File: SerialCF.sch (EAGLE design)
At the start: 17 parts, among them IC1 XR-16C550P, IC2 74LS138N, T1 BC547, T2 BC547

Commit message: Update SerialCF
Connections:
- net A11: now also IC2A.G2A; no longer IC2A.G1
- net GND: now also IC2A.G1
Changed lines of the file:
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@@
 <instance part="P+11" gate="VCC" x="297.18" y="68.58"/>
 <instance part="GND9" gate="1" x="297.18" y="55.88"/>
-<instance part="GND13" gate="1" x="86.36" y="132.08"/>
+<instance part="GND13" gate="1" x="86.36" y="134.62"/>
 <instance part="T2" gate="G$1" x="111.76" y="-15.24"/>
 <instance part="R5" gate="G$1" x="101.6" y="-15.24"/>
@@
 </segment>
 <segment>
-<pinref part="GND13" gate="1" pin="GND"/>
-<wire x1="96.52" y1="134.62" x2="86.36" y2="134.62" width="0.1524" layer="91"/>
-</segment>
-<segment>
 <pinref part="GND3" gate="1" pin="GND"/>
 <pinref part="IC2" gate="P" pin="GND"/>
+</segment>
+<segment>
+<pinref part="IC2" gate="A" pin="G1"/>
+<pinref part="GND13" gate="1" pin="GND"/>
+<wire x1="96.52" y1="137.16" x2="86.36" y2="137.16" width="0.1524" layer="91"/>
 </segment>
 </net>
@@
 <pinref part="IC2" gate="A" pin="B"/>
 <wire x1="96.52" y1="147.32" x2="76.2" y2="147.32" width="0.1524" layer="91"/>
+<label x="88.9" y="147.32" size="1.778" layer="95"/>
 </segment>
 </net>
@@
 <pinref part="IC2" gate="A" pin="C"/>
 <wire x1="96.52" y1="144.78" x2="76.2" y2="144.78" width="0.1524" layer="91"/>
+<label x="88.9" y="144.78" size="1.778" layer="95"/>
 </segment>
 </net>
@@
 </segment>
 <segment>
-<pinref part="IC2" gate="A" pin="G1"/>
-<wire x1="96.52" y1="137.16" x2="76.2" y2="137.16" width="0.1524" layer="91"/>
-</segment>
-</net>
+<pinref part="IC2" gate="A" pin="G2A"/>
+<wire x1="96.52" y1="134.62" x2="91.44" y2="134.62" width="0.1524" layer="91"/>
+<wire x1="91.44" y1="134.62" x2="91.44" y2="129.54" width="0.1524" layer="91"/>
+<wire x1="91.44" y1="129.54" x2="76.2" y2="129.54" width="0.1524" layer="91"/>
+<label x="83.82" y="127" size="1.778" layer="95"/>
+</segment>
+</net>

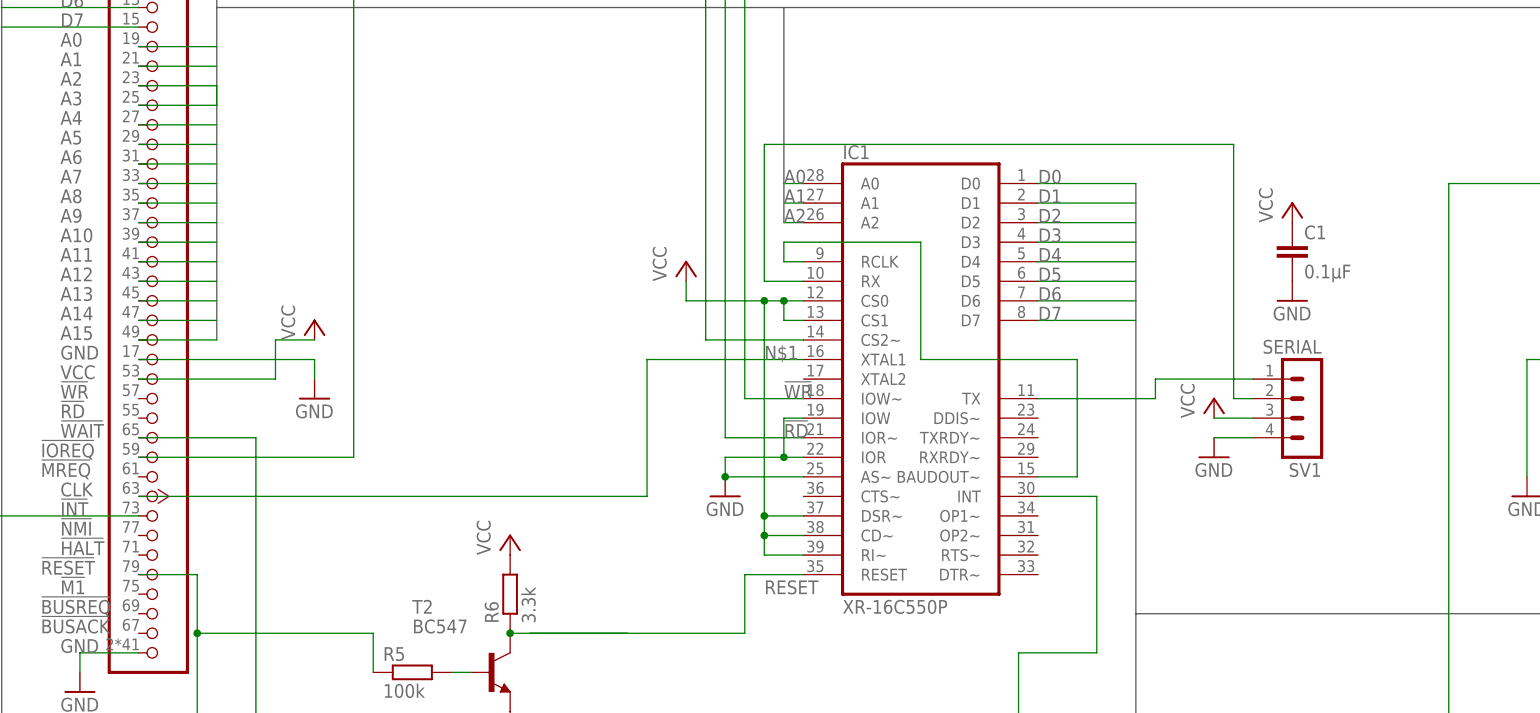
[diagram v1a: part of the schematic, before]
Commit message: Added Oscillator to SerialCF Board. And more Serial Pins
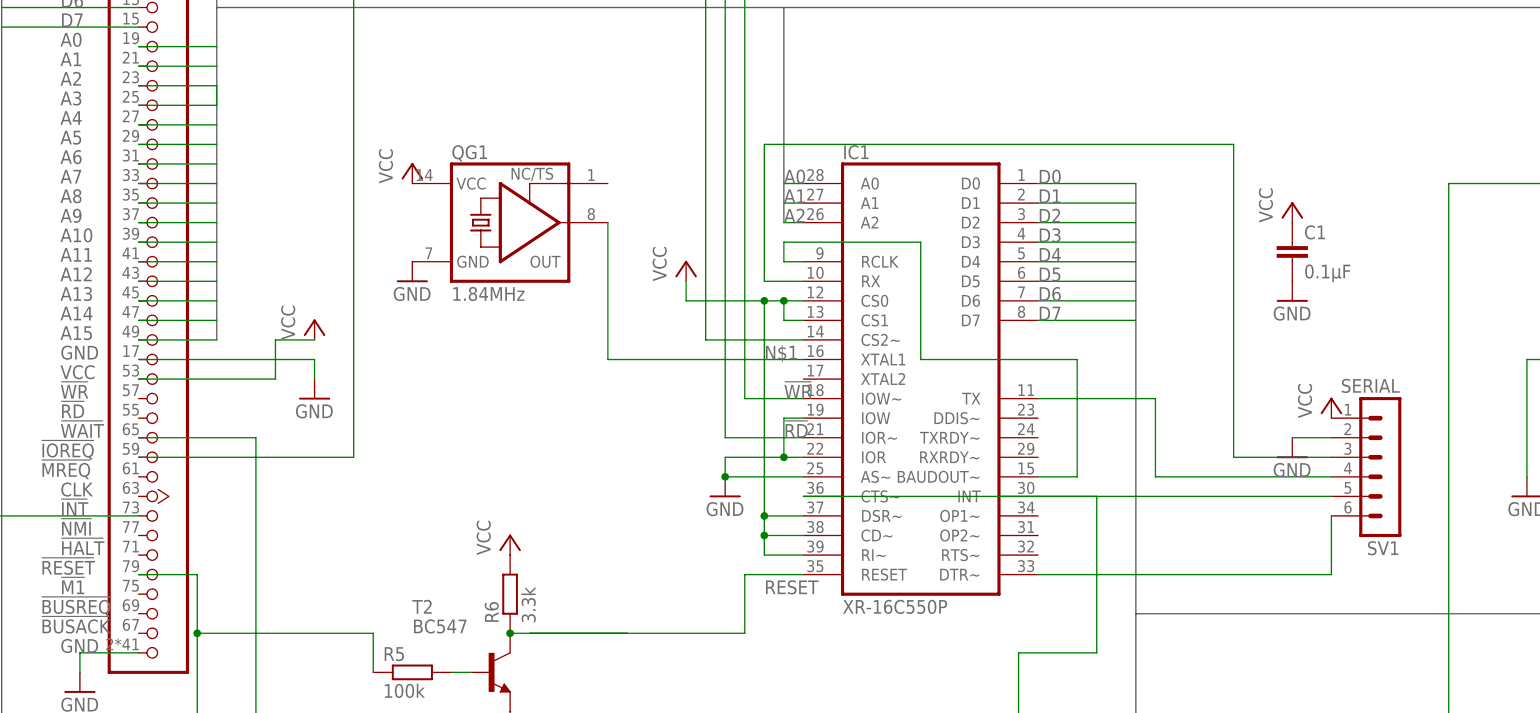
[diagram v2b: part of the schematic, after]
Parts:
- added QG1: 1.84MHz, crystal:XO-14
- SV1: device con-lstb:MA04-1 -> con-lstb:MA06-1
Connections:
- new net N$12: IC1G$1.CTS~, SV1.5
- new net N$14: IC1G$1.DTR~, SV1.6
- net GND: now also QG1.GND, SV1.2; no longer SV1.4
- net N$1: now also QG1.OUT; no longer JP1.CLK
- net N$11: now also SV1.4; no longer SV1.1
- net N$15: now also SV1.3; no longer SV1.2
- net VCC: now also QG1.VCC, SV1.1; no longer SV1.3
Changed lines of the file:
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@@
 <part name="GND7" library="supply1" deviceset="GND" device=""/>
 <part name="P+6" library="supply1" deviceset="VCC" device=""/>
-<part name="SV1" library="con-lstb" deviceset="MA04-1" device="" value="SERIAL"/>
+<part name="SV1" library="con-lstb" deviceset="MA06-1" device="" value="SERIAL"/>
 <part name="P+8" library="supply1" deviceset="VCC" device=""/>
 <part name="GND10" library="supply1" deviceset="GND" device=""/>
@@
 <part name="GND14" library="supply1" deviceset="GND" device=""/>
 <part name="IC2" library="74xx-eu" deviceset="74*138" device="N" technology="LS"/>
+<part name="QG1" library="crystal" deviceset="XO-" device="14" value="1.84MHz"/>
+<part name="P+10" library="supply1" deviceset="VCC" device=""/>
+<part name="GND8" library="supply1" deviceset="GND" device=""/>
 </parts>
 <sheets>
@@
 <instance part="GND7" gate="1" x="142.24" y="7.62"/>
 <instance part="P+6" gate="VCC" x="137.16" y="38.1"/>
-<instance part="SV1" gate="1" x="218.44" y="17.78" rot="R180"/>
-<instance part="P+8" gate="VCC" x="205.74" y="20.32"/>
-<instance part="GND10" gate="1" x="205.74" y="12.7"/>
+<instance part="SV1" gate="1" x="228.6" y="10.16" rot="R180"/>
+<instance part="P+8" gate="VCC" x="220.98" y="20.32"/>
+<instance part="GND10" gate="1" x="215.9" y="12.7"/>
 <instance part="SV2" gate="G$1" x="284.48" y="22.86" rot="R180"/>
 <instance part="R1" gate="G$1" x="299.72" y="2.54">
@@
 <instance part="IC2" gate="A" x="111.76" y="142.24"/>
 <instance part="IC2" gate="P" x="17.78" y="91.44"/>
+<instance part="QG1" gate="G$1" x="114.3" y="43.18"/>
+<instance part="P+10" gate="VCC" x="101.6" y="50.8"/>
+<instance part="GND8" gate="1" x="101.6" y="35.56"/>
 </instances>
 <busses>
@@
 </segment>
 <segment>
-<pinref part="SV1" gate="1" pin="3"/>
-<pinref part="P+8" gate="VCC" pin="VCC"/>
-<wire x1="210.82" y1="17.78" x2="205.74" y2="17.78" width="0.1524" layer="91"/>
-</segment>
-<segment>
 <pinref part="P+9" gate="VCC" pin="VCC"/>
 <wire x1="307.34" y1="33.02" x2="307.34" y2="25.4" width="0.1524" layer="91"/>
@@
 <pinref part="P+1" gate="VCC" pin="VCC"/>
 <pinref part="IC2" gate="P" pin="VCC"/>
+</segment>
+<segment>
+<pinref part="QG1" gate="G$1" pin="VCC"/>
+<pinref part="P+10" gate="VCC" pin="VCC"/>
+</segment>
+<segment>
+<pinref part="SV1" gate="1" pin="1"/>
+<pinref part="P+8" gate="VCC" pin="VCC"/>
 </segment>
 </net>
@@
 <wire x1="152.4" y1="10.16" x2="142.24" y2="10.16" width="0.1524" layer="91"/>
 <junction x="142.24" y="10.16"/>
-</segment>
-<segment>
-<pinref part="SV1" gate="1" pin="4"/>
-<pinref part="GND10" gate="1" pin="GND"/>
-<wire x1="210.82" y1="15.24" x2="205.74" y2="15.24" width="0.1524" layer="91"/>
 </segment>
 <segment>
@@
 <wire x1="96.52" y1="137.16" x2="86.36" y2="137.16" width="0.1524" layer="91"/>
 </segment>
+<segment>
+<pinref part="QG1" gate="G$1" pin="GND"/>
+<pinref part="GND8" gate="1" pin="GND"/>
+</segment>
+<segment>
+<pinref part="GND10" gate="1" pin="GND"/>
+<pinref part="SV1" gate="1" pin="2"/>
+<wire x1="215.9" y1="15.24" x2="220.98" y2="15.24" width="0.1524" layer="91"/>
+</segment>
 </net>
 <net name="!WR" class="0">
@@
 <net name="N$11" class="0">
 <segment>
-<pinref part="SV1" gate="1" pin="1"/>
 <pinref part="IC1" gate="G$1" pin="TX"/>
 <wire x1="182.88" y1="20.32" x2="198.12" y2="20.32" width="0.1524" layer="91"/>
-<wire x1="198.12" y1="20.32" x2="198.12" y2="22.86" width="0.1524" layer="91"/>
-<wire x1="198.12" y1="22.86" x2="210.82" y2="22.86" width="0.1524" layer="91"/>
+<pinref part="SV1" gate="1" pin="4"/>
+<wire x1="220.98" y1="10.16" x2="198.12" y2="10.16" width="0.1524" layer="91"/>
+<wire x1="198.12" y1="10.16" x2="198.12" y2="20.32" width="0.1524" layer="91"/>
 </segment>
 </net>
@@
 <wire x1="147.32" y1="35.56" x2="147.32" y2="53.34" width="0.1524" layer="91"/>
 <wire x1="147.32" y1="53.34" x2="208.28" y2="53.34" width="0.1524" layer="91"/>
-<wire x1="208.28" y1="53.34" x2="208.28" y2="20.32" width="0.1524" layer="91"/>
-<pinref part="SV1" gate="1" pin="2"/>
-<wire x1="208.28" y1="20.32" x2="210.82" y2="20.32" width="0.1524" layer="91"/>
+<wire x1="208.28" y1="53.34" x2="208.28" y2="12.7" width="0.1524" layer="91"/>
+<pinref part="SV1" gate="1" pin="3"/>
+<wire x1="208.28" y1="12.7" x2="220.98" y2="12.7" width="0.1524" layer="91"/>
 </segment>
 </net>
@@
 <segment>
 <pinref part="IC1" gate="G$1" pin="XTAL1"/>
-<wire x1="152.4" y1="25.4" x2="132.08" y2="25.4" width="0.1524" layer="91"/>
-<wire x1="132.08" y1="25.4" x2="132.08" y2="7.62" width="0.1524" layer="91"/>
-<pinref part="JP1" gate="A" pin="CLK"/>
-<wire x1="66.04" y1="7.62" x2="132.08" y2="7.62" width="0.1524" layer="91"/>
+<wire x1="152.4" y1="25.4" x2="127" y2="25.4" width="0.1524" layer="91"/>
 <label x="147.32" y="25.4" size="1.778" layer="95"/>
+<pinref part="QG1" gate="G$1" pin="OUT"/>
+<wire x1="127" y1="25.4" x2="127" y2="43.18" width="0.1524" layer="91"/>
 </segment>
 </net>
@@
 </segment>
 </net>
+<net name="N$12" class="0">
+<segment>
+<pinref part="IC1" gate="G$1" pin="CTS~"/>
+<pinref part="SV1" gate="1" pin="5"/>
+<wire x1="152.4" y1="7.62" x2="220.98" y2="7.62" width="0.1524" layer="91"/>
+</segment>
+</net>
+<net name="N$14" class="0">
+<segment>
+<pinref part="IC1" gate="G$1" pin="DTR~"/>
+<pinref part="SV1" gate="1" pin="6"/>
+<wire x1="182.88" y1="-2.54" x2="220.98" y2="-2.54" width="0.1524" layer="91"/>
+<wire x1="220.98" y1="-2.54" x2="220.98" y2="5.08" width="0.1524" layer="91"/>
+</segment>
+</net>

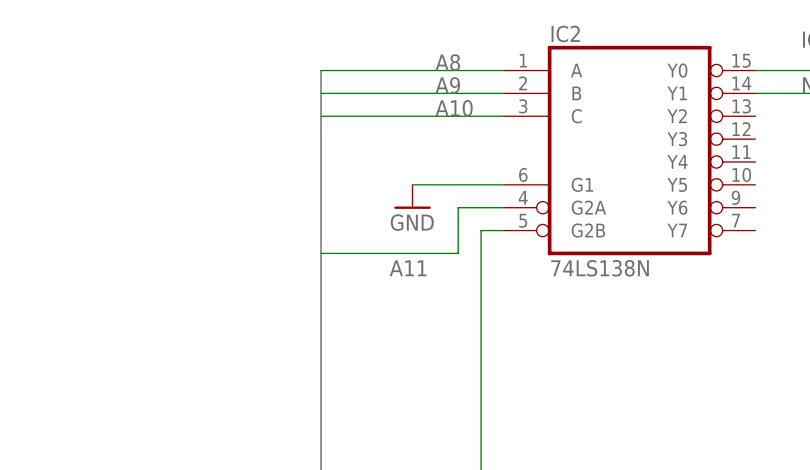
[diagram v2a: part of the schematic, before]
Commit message: Fix stupid VCC/GND mistakes on Address decoder
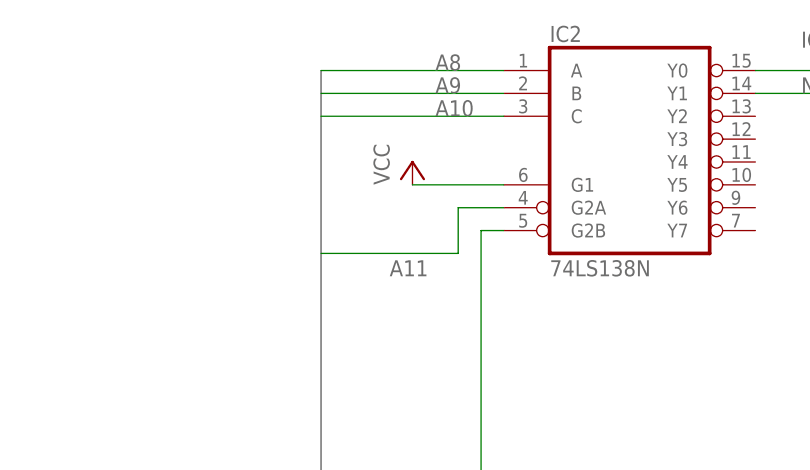
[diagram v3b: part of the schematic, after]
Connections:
- net GND: no longer IC2A.G1
- net VCC: now also IC2A.G1
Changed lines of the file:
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@@
 <part name="P+11" library="supply1" deviceset="VCC" device=""/>
 <part name="GND9" library="supply1" deviceset="GND" device=""/>
-<part name="GND13" library="supply1" deviceset="GND" device=""/>
 <part name="T2" library="transistor" deviceset="BC547" device=""/>
 <part name="R5" library="resistor" deviceset="R-EU_" device="0207/2V" value="100k"/>
@@
 <part name="P+10" library="supply1" deviceset="VCC" device=""/>
 <part name="GND8" library="supply1" deviceset="GND" device=""/>
+<part name="P+12" library="supply1" deviceset="VCC" device=""/>
 </parts>
 <sheets>
@@
 <instance part="P+11" gate="VCC" x="297.18" y="68.58"/>
 <instance part="GND9" gate="1" x="297.18" y="55.88"/>
-<instance part="GND13" gate="1" x="86.36" y="134.62"/>
 <instance part="T2" gate="G$1" x="111.76" y="-15.24"/>
 <instance part="R5" gate="G$1" x="101.6" y="-15.24"/>
@@
 <instance part="P+10" gate="VCC" x="101.6" y="50.8"/>
 <instance part="GND8" gate="1" x="101.6" y="35.56"/>
+<instance part="P+12" gate="VCC" x="86.36" y="139.7"/>
 </instances>
 <busses>
@@
 <pinref part="SV1" gate="1" pin="1"/>
 <pinref part="P+8" gate="VCC" pin="VCC"/>
+</segment>
+<segment>
+<pinref part="IC2" gate="A" pin="G1"/>
+<wire x1="96.52" y1="137.16" x2="86.36" y2="137.16" width="0.1524" layer="91"/>
+<pinref part="P+12" gate="VCC" pin="VCC"/>
 </segment>
 </net>
@@
 </segment>
 <segment>
-<pinref part="IC2" gate="A" pin="G1"/>
-<pinref part="GND13" gate="1" pin="GND"/>
-<wire x1="96.52" y1="137.16" x2="86.36" y2="137.16" width="0.1524" layer="91"/>
-</segment>
-<segment>

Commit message: Add pullup
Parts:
- added R7: 3.3k, resistor:R-EU_0207/2V
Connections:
- net !RESET: now also R7.1
- net IOCS1: now also IC2A.Y0
- net N$5: now also IC2A.G2B
- net VCC: now also R7.2
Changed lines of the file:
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@@
 <part name="GND8" library="supply1" deviceset="GND" device=""/>
 <part name="P+12" library="supply1" deviceset="VCC" device=""/>
+<part name="R7" library="resistor" deviceset="R-EU_" device="0207/2V" value="3.3k"/>
+<part name="P+14" library="supply1" deviceset="VCC" device=""/>
 </parts>
 <sheets>
@@
 <instance part="GND8" gate="1" x="101.6" y="35.56"/>
 <instance part="P+12" gate="VCC" x="86.36" y="139.7"/>
+<instance part="R7" gate="G$1" x="91.44" y="-5.08" rot="R90"/>
+<instance part="P+14" gate="VCC" x="91.44" y="2.54"/>
 </instances>
 <busses>
@@
 <wire x1="96.52" y1="137.16" x2="86.36" y2="137.16" width="0.1524" layer="91"/>
 <pinref part="P+12" gate="VCC" pin="VCC"/>
+</segment>
+<segment>
+<pinref part="R7" gate="G$1" pin="2"/>
+<pinref part="P+14" gate="VCC" pin="VCC"/>
 </segment>
 </net>
@@
 <wire x1="73.66" y1="-2.54" x2="73.66" y2="-10.16" width="0.1524" layer="91"/>
 <wire x1="73.66" y1="-10.16" x2="73.66" y2="-30.48" width="0.1524" layer="91"/>
-<wire x1="73.66" y1="-10.16" x2="96.52" y2="-10.16" width="0.1524" layer="91"/>
+<wire x1="73.66" y1="-10.16" x2="91.44" y2="-10.16" width="0.1524" layer="91"/>
 <junction x="73.66" y="-10.16"/>
+<wire x1="91.44" y1="-10.16" x2="96.52" y2="-10.16" width="0.1524" layer="91"/>
 <wire x1="96.52" y1="-10.16" x2="96.52" y2="-15.24" width="0.1524" layer="91"/>
+<pinref part="R7" gate="G$1" pin="1"/>
+<junction x="91.44" y="-10.16"/>
 </segment>
 </net>
@@
 <wire x1="264.16" y1="2.54" x2="264.16" y2="149.86" width="0.1524" layer="91"/>
 <label x="129.54" y="152.4" size="1.778" layer="95"/>
+<pinref part="IC2" gate="A" pin="Y0"/>
 </segment>
 </net>
@@
 <pinref part="JP1" gate="A" pin="!IOREQ"/>
 <wire x1="66.04" y1="12.7" x2="93.98" y2="12.7" width="0.1524" layer="91"/>
-</segment>
-</net>
+<pinref part="IC2" gate="A" pin="G2B"/>
+</segment>
+</net>
